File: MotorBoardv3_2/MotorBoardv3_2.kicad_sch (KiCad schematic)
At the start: 80 parts, among them J1 Bump0, J11 GP2Y0A41SK0F, J12 GP2Y0A41SK0F, J13 GP2Y0A41SK0F, J15 7.2, J16 LP5.0, J17 ELA, J18 ERA, J19 Voltage Display Port, J2 Bump1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

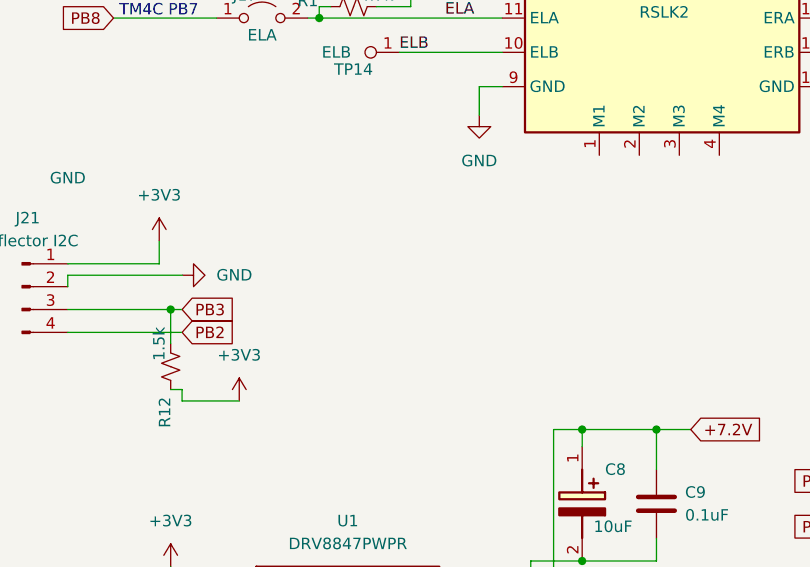
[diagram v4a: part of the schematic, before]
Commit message: Added reflector sensor support pins to schematic and layout
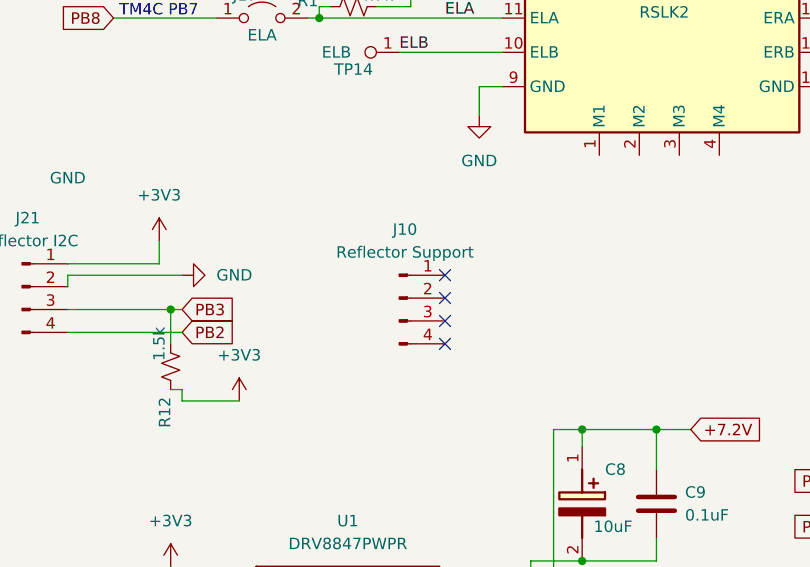
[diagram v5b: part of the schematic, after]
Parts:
- added J10: Reflector Support, Connector_PinHeader_2.54mm:PinHeader_1x04_P2.54mm_Vertical, symbol Connector:Conn_01x04_Pin
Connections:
- no-connect marks 0 -> 4
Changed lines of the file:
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@@
 		(color 0 0 0 0)
 	)
+	(no_connect
+		(at 138.43 121.92)
+	)
+	(no_connect
+		(at 138.43 124.46)
+	)
+	(no_connect
+		(at 138.43 127)
+	)
+	(no_connect
+		(at 138.43 129.54)
+	)
 	(wire
 		(pts
@@
 					(unit 1)
 				)
+			)
+		)
+	)
+	(symbol
+		(lib_id "Connector:Conn_01x04_Pin")
+		(at 133.35 124.46 0)
+		(unit 1)
+		(exclude_from_sim no)
+		(in_bom yes)
+		(on_board yes)
+		(dnp no)
+		(fields_autoplaced yes)
+		(property "Reference" "J10"
+			(at 133.985 116.84 0)
+			(effects
+				(font
+					(size 1.27 1.27)
+				)
+			)
+		)
+		(property "Value" "Reflector Support"
+			(at 133.985 119.38 0)
+			(effects
+				(font
+					(size 1.27 1.27)
+				)
+			)
+		)
+		(property "Footprint" "Connector_PinHeader_2.54mm:PinHeader_1x04_P2.54mm_Vertical"
+			(at 133.35 124.46 0)
+			(effects
+				(font
+					(size 1.27 1.27)
+				)
+				(hide yes)
+			)
+		)
+		(property "Datasheet" "~"
+			(at 133.35 124.46 0)
+			(effects
+				(font
+					(size 1.27 1.27)
+				)
+				(hide yes)
+			)
+		)
+		(property "Description" "Generic connector, single row, 01x04, script generated"
+			(at 133.35 124.46 0)
+			(effects
+				(font
+					(size 1.27 1.27)
+				)
+				(hide yes)
+			)
+		)
+		(pin "4"
+		)
+		(pin "3"
+		)
+		(pin "2"
+		)
+		(pin "1"
+		)
+		(instances
+			(project "MotorBoardv3_2"
+				(path "/69b823fd-c065-40ff-9bb9-c5835555f3eb"
+					(reference "J10")
+					(unit 1)
+				)

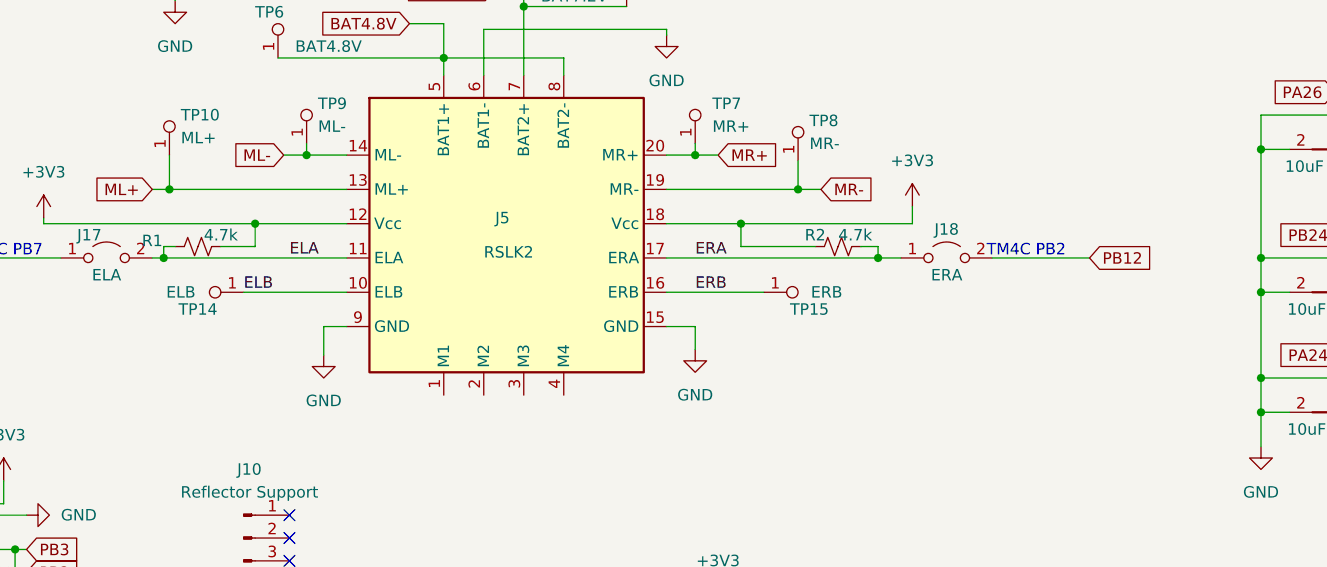
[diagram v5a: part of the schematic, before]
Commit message: Changed pin usages for rev 2
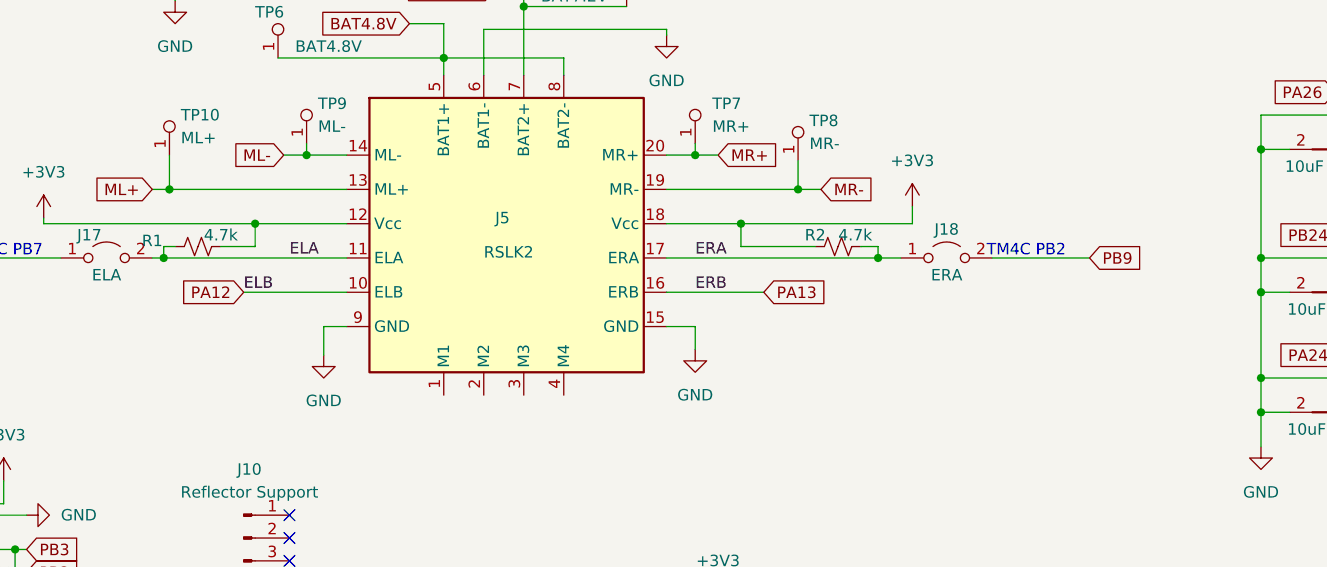
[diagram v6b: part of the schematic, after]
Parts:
- removed TP14: ELB, RSLK2:Testpoint_1x1, symbol RSLK2:Testpoint_1
- removed TP15: ERB, RSLK2:Testpoint_1x1, symbol RSLK2:Testpoint_1
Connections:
- net ELB is gone; now on net PA12: J5.10 (ELB)
- net ERB is gone; now on net PA13: J5.16 (ERB)
- net PB12: no longer J18.2 (B)
- net PB9: now also J18.2 (B)
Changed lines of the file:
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@@
 	(label "ELB"
 		(at 133.35 97.155 0)
+		(fields_autoplaced yes)
 		(effects
 			(font
@@
 	(label "PushButton_1"
 		(at 180.34 13.97 180)
+		(fields_autoplaced yes)
 		(effects
 			(font
@@
 	(label "PushButton_2"
 		(at 180.34 33.02 180)
+		(fields_autoplaced yes)
 		(effects
 			(font
@@
 	(label "ELA"
 		(at 138.43 93.345 0)
+		(fields_autoplaced yes)
 		(effects
 			(font
@@
 	(label "ERA"
 		(at 183.515 93.345 0)
+		(fields_autoplaced yes)
 		(effects
 			(font
@@
 	(label "PushButton_1"
 		(at 220.98 13.97 0)
+		(fields_autoplaced yes)
 		(effects
 			(font
@@
 	(label "LP3_3"
 		(at 20.32 24.13 0)
+		(fields_autoplaced yes)
 		(effects
 			(font
@@
 	(label "PushButton_2"
 		(at 220.98 21.59 0)
+		(fields_autoplaced yes)
 		(effects
 			(font
@@
 	(label "ERB"
 		(at 183.515 97.155 0)
+		(fields_autoplaced yes)
 		(effects
 			(font
@@
 	(label "PushButton_2"
 		(at 119.38 34.29 180)
+		(fields_autoplaced yes)
 		(effects
 			(font
@@
 	(label "VBUS"
 		(at 48.895 19.05 0)
+		(fields_autoplaced yes)
 		(effects
 			(font
@@
 	(label "PushButton_1"
 		(at 119.38 31.75 180)
+		(fields_autoplaced yes)
 		(effects
 			(font
@@
 		)
 	)
+	(global_label "PA13"
+		(shape input)
+		(at 191.135 97.155 0)
+		(fields_autoplaced yes)
+		(effects
+			(font
+				(size 1.27 1.27)
+			)
+			(justify left)
+		)
+		(property "Intersheetrefs" "${INTERSHEET_REFS}"
+			(at 198.8978 97.155 0)
+			(effects
+				(font
+					(size 1.27 1.27)
+				)
+				(justify left)
+				(hide yes)
+			)
+		)
+	)
 	(global_label "PB4"
 		(shape input)
@@
 		)
 	)
-	(global_label "PB12"
+	(global_label "PB9"
 		(shape input)
 		(at 227.33 93.345 0)
@@
 		)
 		(property "Intersheetrefs" "${INTERSHEET_REFS}"
-			(at 235.2742 93.345 0)
+			(at 234.0647 93.345 0)
 			(effects
 				(font
@@
 		)
 	)
+	(global_label "PA12"
+		(shape input)
+		(at 133.35 97.155 180)
+		(fields_autoplaced yes)
+		(effects
+			(font
+				(size 1.27 1.27)
+			)
+			(justify right)
+		)
+		(property "Intersheetrefs" "${INTERSHEET_REFS}"
+			(at 125.5872 97.155 0)
+			(effects
+				(font
+					(size 1.27 1.27)
+				)
+				(justify right)
+				(hide yes)
+			)
+		)
+	)
 	(global_label "PB1"
 		(shape input)
@@
 	)
 	(symbol
-		(lib_id "RSLK2:Testpoint_1")
-		(at 133.35 95.25 90)
-		(unit 1)
-		(exclude_from_sim no)
-		(in_bom yes)
-		(on_board yes)
-		(dnp no)
-		(property "Reference" "TP14"
-			(at 128.27 99.06 90)
-			(effects
-				(font
-					(size 1.27 1.27)
-				)
-			)
-		)
-		(property "Value" "ELB"
-			(at 126.365 97.155 90)
-			(effects
-				(font
-					(size 1.27 1.27)
-				)
-			)
-		)
-		(property "Footprint" "RSLK2:Testpoint_1x1"
-			(at 127.635 95.25 0)
-			(effects
-				(font
-					(size 1.27 1.27)
-				)
-				(hide yes)
-			)
-		)
-		(property "Datasheet" "~"
-			(at 133.35 95.25 0)
-			(effects
-				(font
-					(size 1.27 1.27)
-				)
-				(hide yes)
-			)
-		)
-		(property "Description" "Testpoint"
-			(at 133.35 95.25 0)
-			(effects
-				(font
-					(size 1.27 1.27)
-				)
-				(hide yes)
-			)
-		)
-		(pin "1"
-		)
-		(instances
-			(project "MotorBoardv3_2"
-				(path "/69b823fd-c065-40ff-9bb9-c5835555f3eb"
-					(reference "TP14")
-					(unit 1)
-				)
-			)
-		)
-	)
-	(symbol
 		(lib_id "RSLK2:SSD1306")
 		(at 222.885 146.685 0)
@@
 					(unit 1)
 				)
-			)
-		)
-	)
-	(symbol
-		(lib_id "RSLK2:Testpoint_1")
-		(at 191.135 95.25 270)
-		(mirror x)
-		(unit 1)
-		(exclude_from_sim no)
-		(in_bom yes)
-		(on_board yes)
-		(dnp no)
-		(property "Reference" "TP15"
-			(at 196.215 99.06 90)
-			(effects
-				(font
-					(size 1.27 1.27)
-				)
-			)
-		)
-		(property "Value" "ERB"
-			(at 198.12 97.155 90)
-			(effects
-				(font
-					(size 1.27 1.27)
-				)
-			)
-		)
-		(property "Footprint" "RSLK2:Testpoint_1x1"
-			(at 196.85 95.25 0)
-			(effects
-				(font
-					(size 1.27 1.27)
-				)
-				(hide yes)
-			)
-		)
-		(property "Datasheet" "~"
-			(at 191.135 95.25 0)
-			(effects
-				(font
-					(size 1.27 1.27)
-				)
-				(hide yes)
-			)
-		)
-		(property "Description" "Testpoint"
-			(at 191.135 95.25 0)
-			(effects
-				(font
-					(size 1.27 1.27)
-				)
-				(hide yes)
-			)
-		)
-		(pin "1"
-		)
-		(instances
-			(project "MotorBoardv3_2"
-				(path "/69b823fd-c065-40ff-9bb9-c5835555f3eb"
-					(reference "TP15")
-					(unit 1)
-				)

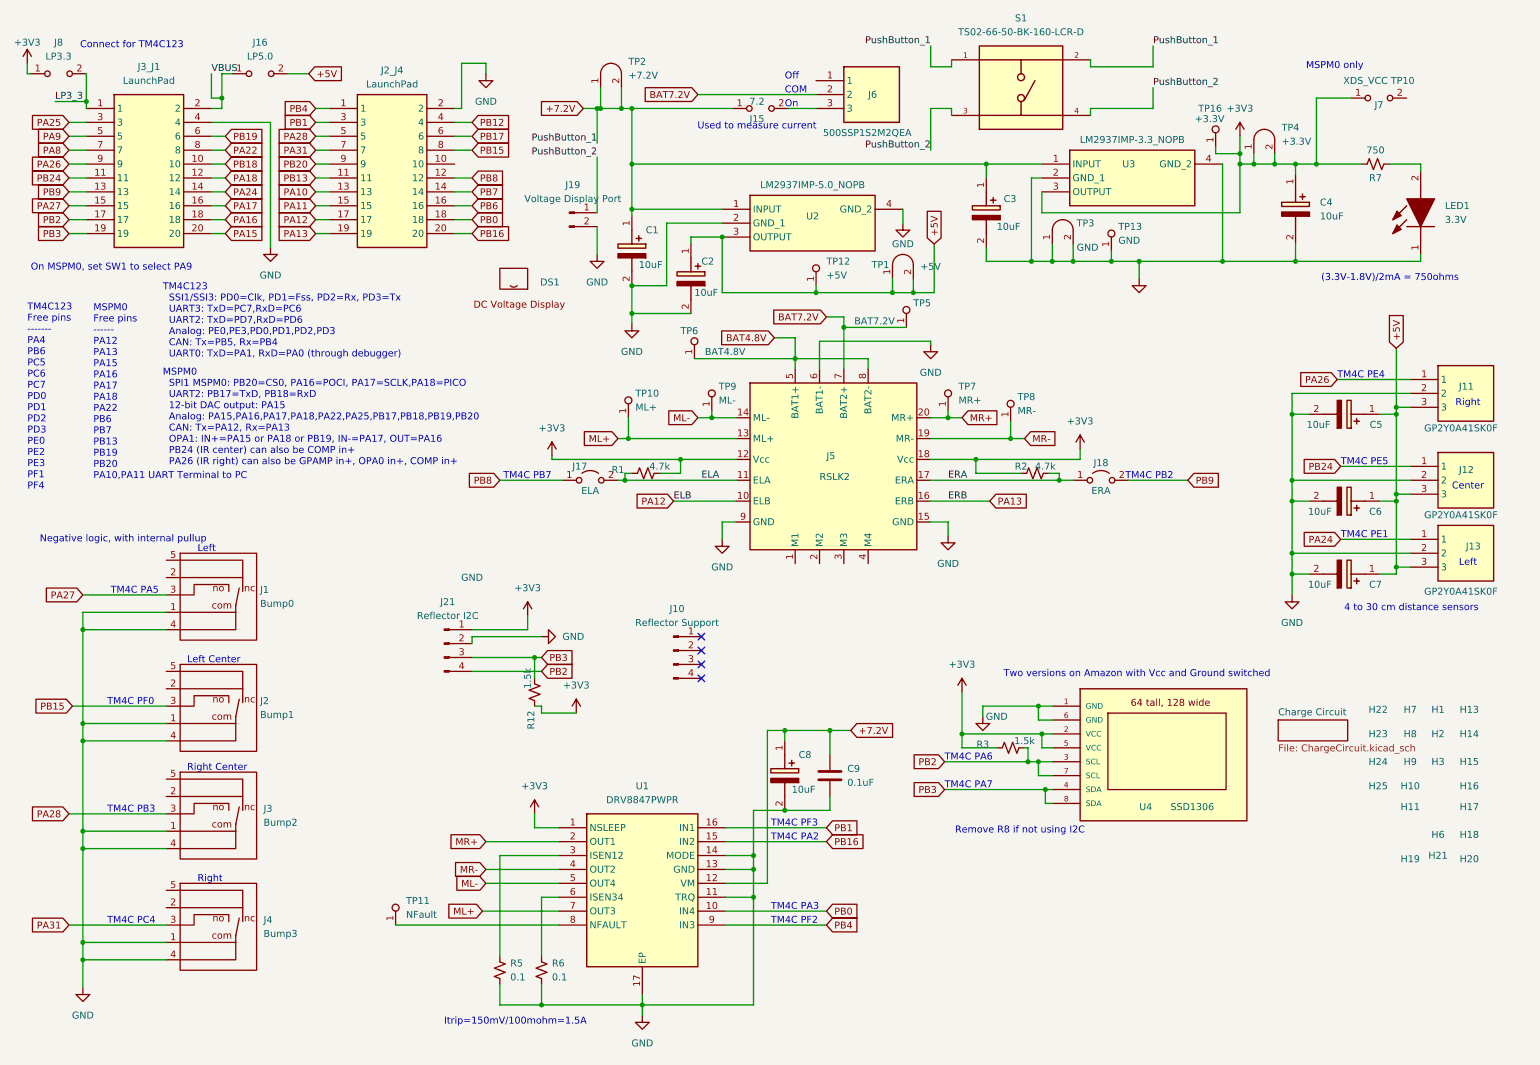
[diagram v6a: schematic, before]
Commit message: added pullup resistors to encoders
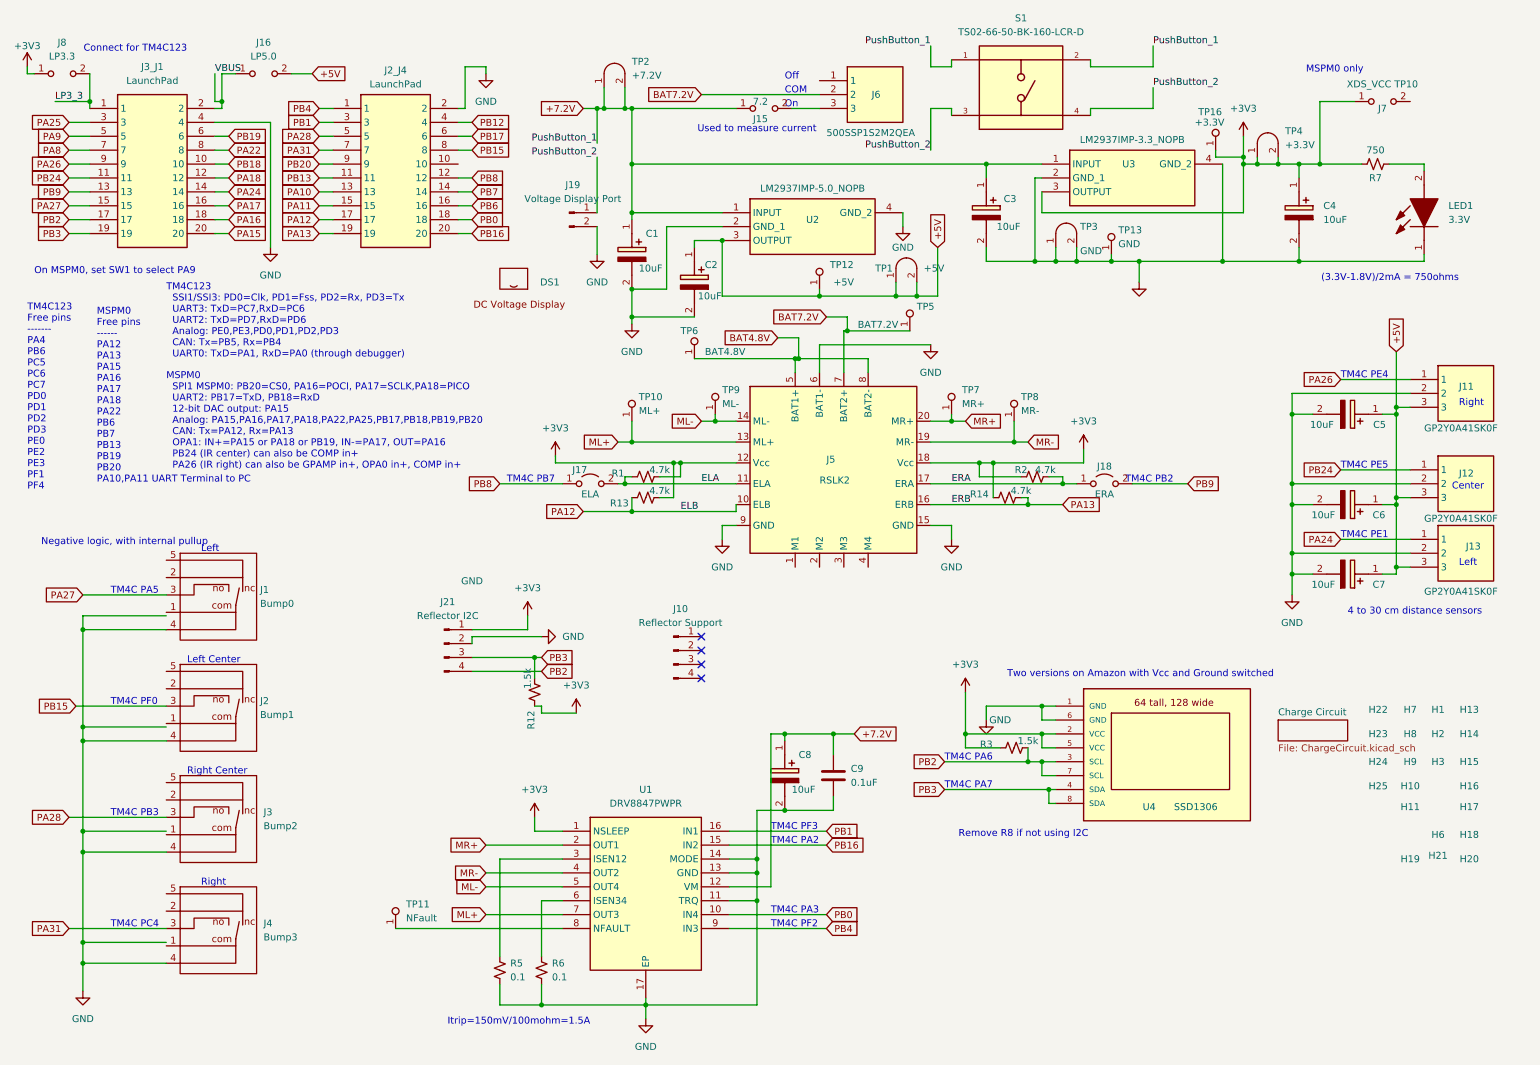
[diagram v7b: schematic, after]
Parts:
- added R13, R14: 4.7k, RSLK2:R_0603_1608Metric, symbol RSLK2:R_0603
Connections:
- net +3V3: now also R13.2, R14.1
- net GND: no longer J1.1 (com), J2.1 (com), J3.1 (com), J4.1 (com)
- net PA12: now also R13.1
- net PA13: now also R14.2
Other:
- moved on the sheet: C1, C2, C4, C5, C6, C7, C9, J12, J15, J16, J17, J18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
